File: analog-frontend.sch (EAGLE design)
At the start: 70 parts, among them IC1 TPS63031, IC2 ADG731, IC3 TM4C123G, IC4 INA332, IC5 NRF24L01SMD, IC6 OPA2320, Y1 CRYSTAL3X2, Y2 CRYSTAL3X2

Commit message: final files send for fab.
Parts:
- removed R16: (no value), FAB_Hello:RESISTOR0402
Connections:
- net AIN: now also IC3A.PB5; no longer IC5.PB5
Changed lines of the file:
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@@
 <part name="R3" library="rcl" deviceset="R-US_" device="R0402"/>
 <part name="SUPPLY25" library="supply2" deviceset="GND" device=""/>
-<part name="R16" library="FAB_Hello" deviceset="RESISTOR" device="0402"/>
 </parts>
 <sheets>
@@
 <instance part="R3" gate="G$1" x="149.86" y="68.58" rot="R90"/>
 <instance part="SUPPLY25" gate="GND" x="149.86" y="55.88"/>
-<instance part="R16" gate="G$1" x="116.84" y="149.86"/>
 </instances>
 <busses>
@@
 <wire x1="340.36" y1="233.68" x2="340.36" y2="226.06" width="0.1524" layer="91"/>
 <junction x="340.36" y="226.06"/>
+<label x="340.36" y="241.3" size="1.27" layer="95" rot="R90" xref="yes"/>
 <wire x1="340.36" y1="233.68" x2="340.36" y2="241.3" width="0.1524" layer="91"/>
 <junction x="340.36" y="233.68"/>
-<wire x1="340.36" y1="241.3" x2="342.9" y2="241.3" width="0.1524" layer="91"/>
-<label x="342.9" y="241.3" size="1.27" layer="95" xref="yes"/>
-</segment>
-<segment>
-<pinref part="IC5" gate="A" pin="PB5"/>
-<wire x1="213.36" y1="121.92" x2="220.98" y2="121.92" width="0.1524" layer="91"/>
-<label x="220.98" y="121.92" size="1.27" layer="95" xref="yes"/>
+</segment>
+<segment>
+<pinref part="IC3" gate="A" pin="PB5"/>
+<wire x1="213.36" y1="121.92" x2="223.52" y2="121.92" width="0.1524" layer="91"/>
+<wire x1="223.52" y1="121.92" x2="223.52" y2="134.62" width="0.1524" layer="91"/>
+<label x="223.52" y="134.62" size="1.27" layer="95" rot="R90" xref="yes"/>
 </segment>
 </net>
@@
 </segment>
 </net>
-<net name="N$57" class="0">
-<segment>
-<wire x1="228.6" y1="106.68" x2="228.6" y2="101.6" width="0.1524" layer="91"/>
-</segment>
-</net>

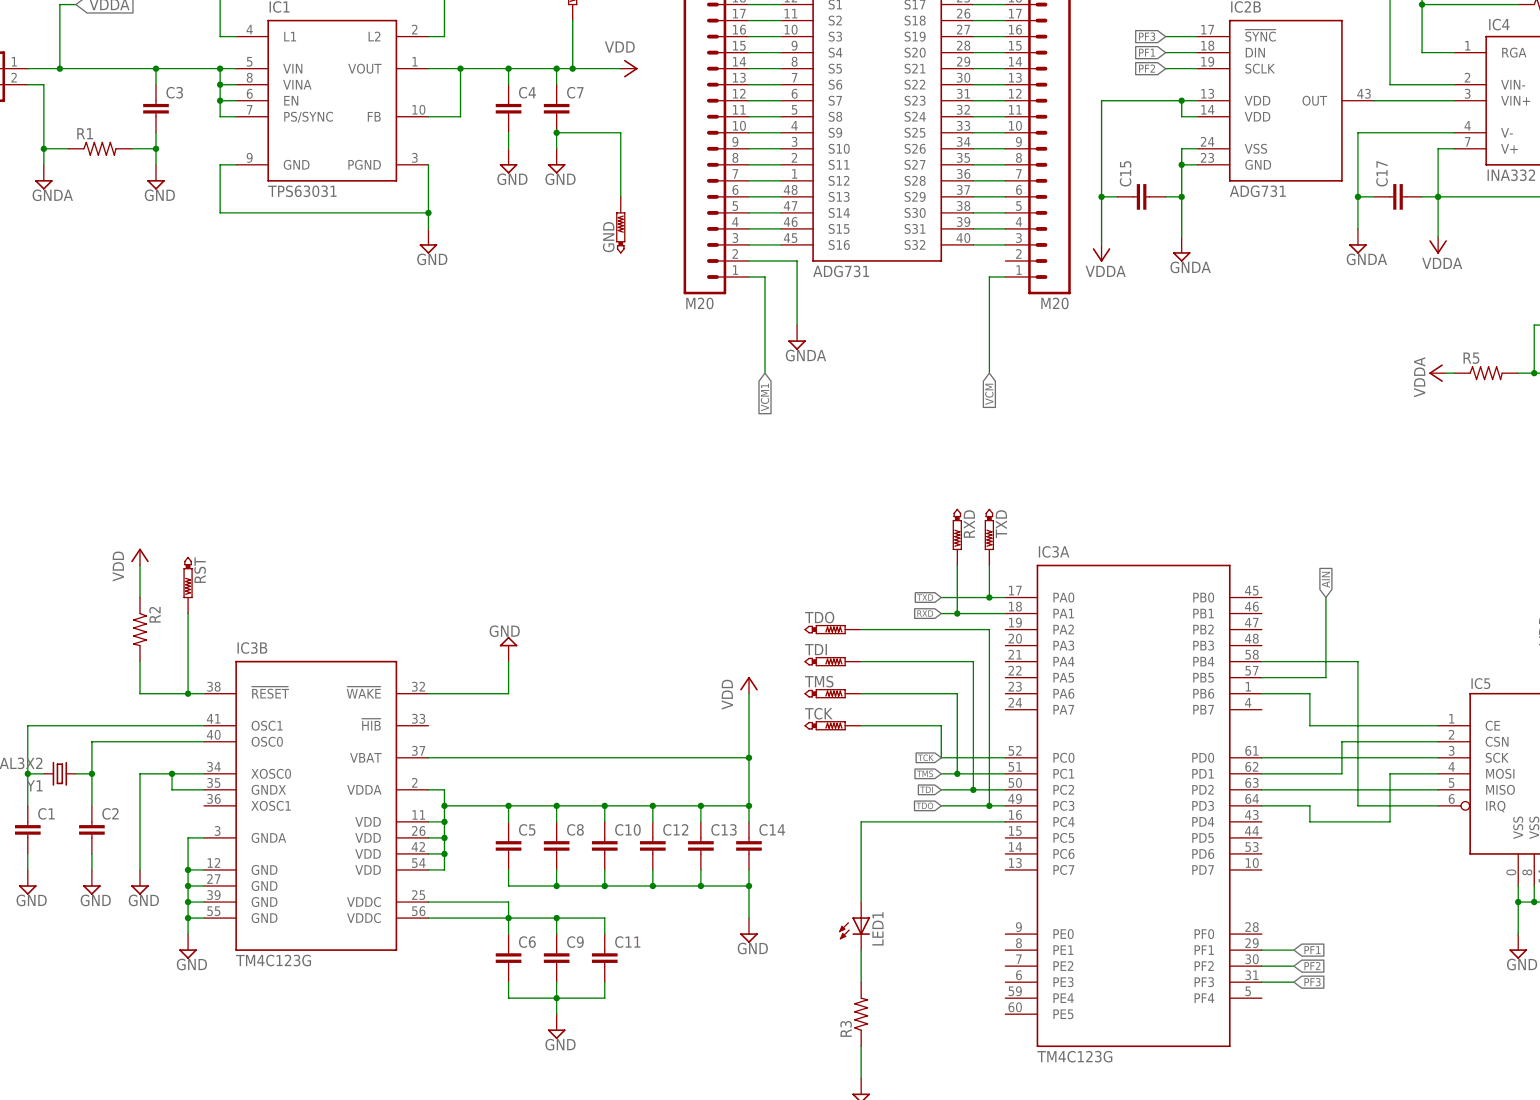
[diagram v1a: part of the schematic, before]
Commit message: added component values
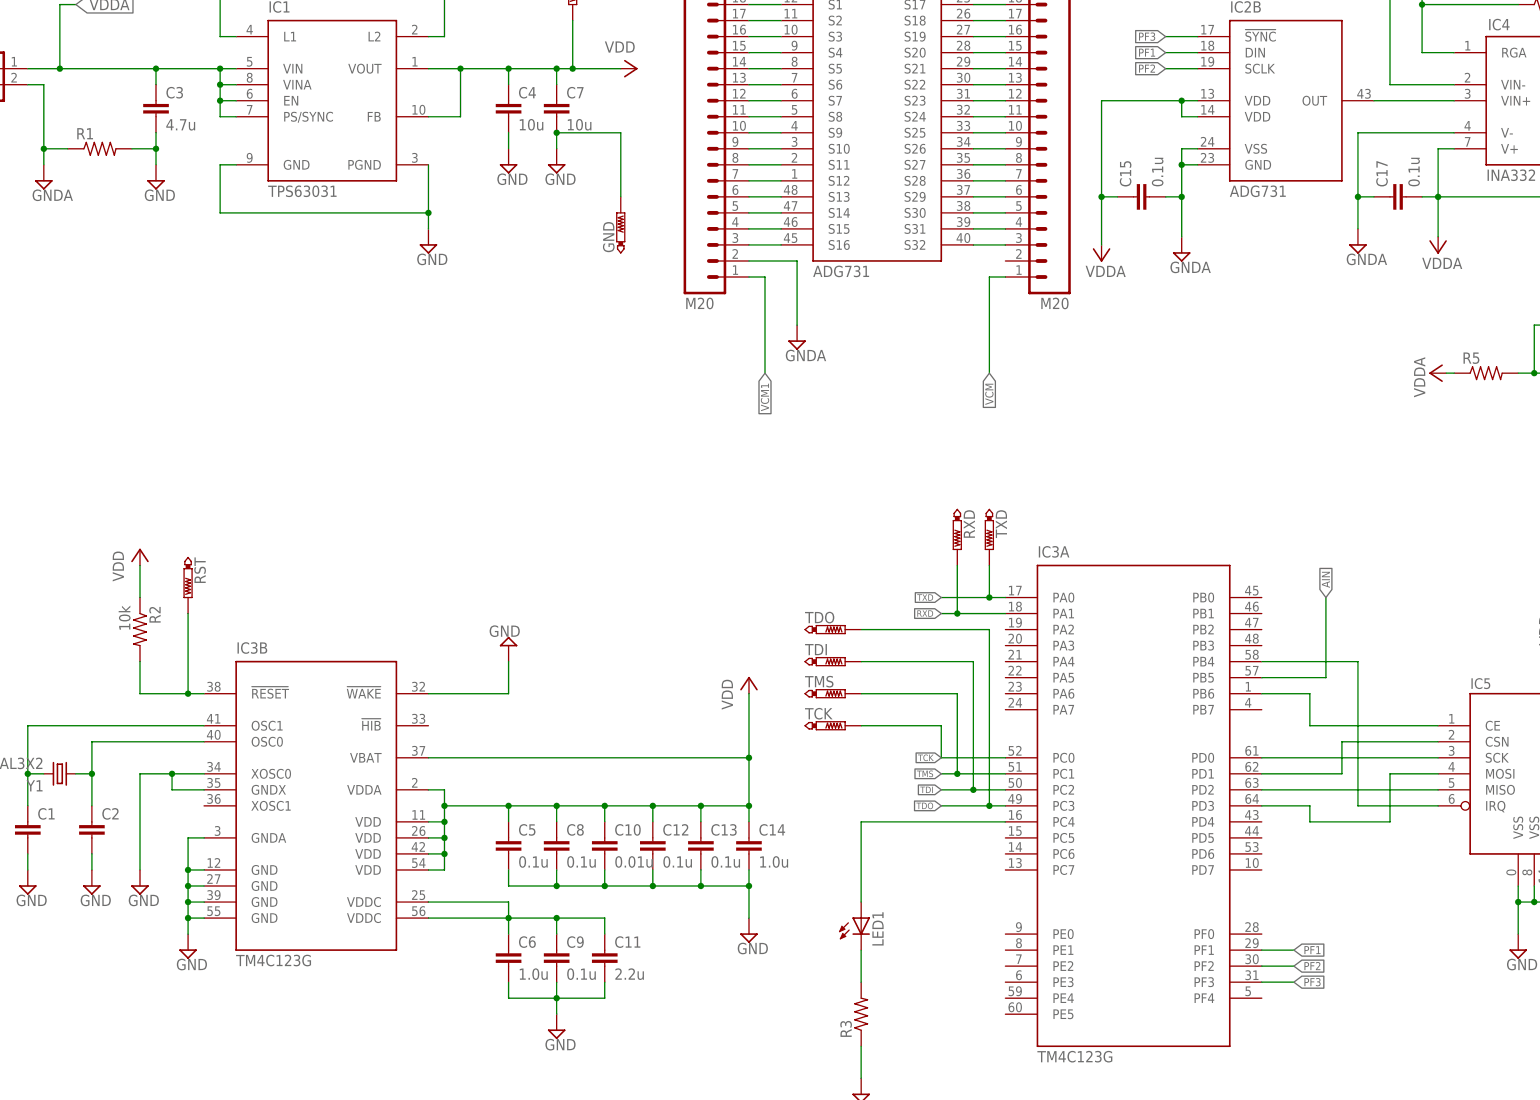
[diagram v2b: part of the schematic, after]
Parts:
- C10: value (none) -> 0.01u
- C11: value (none) -> 2.2u
- C12, C13, C15, C17, C5, C8, C9: value (none) -> 0.1u
- C14, C6: value (none) -> 1.0u
- C3: value (none) -> 4.7u
- C4, C7: value (none) -> 10u
- R2: value (none) -> 10k
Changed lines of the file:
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@@
 <?xml version="1.0" encoding="utf-8"?>
 <!DOCTYPE eagle SYSTEM "eagle.dtd">
-<eagle version="6.5.0">
+<eagle version="6.6.0">
 <drawing>
 <settings>
@@
 <part name="IC1" library="mor307" deviceset="TPS63031" device=""/>
 <part name="L1" library="mor307" deviceset="VLS25201" device=""/>
-<part name="C3" library="rcl" deviceset="C-EU" device="C0402"/>
-<part name="C4" library="rcl" deviceset="C-EU" device="C0402"/>
+<part name="C3" library="rcl" deviceset="C-EU" device="C0402" value="4.7u"/>
+<part name="C4" library="rcl" deviceset="C-EU" device="C0402" value="10u"/>
 <part name="SUPPLY1" library="supply2" deviceset="GND" device=""/>
 <part name="SUPPLY2" library="supply2" deviceset="GND" device=""/>
 <part name="SUPPLY3" library="supply2" deviceset="GND" device=""/>
-<part name="C7" library="rcl" deviceset="C-EU" device="C0402"/>
+<part name="C7" library="rcl" deviceset="C-EU" device="C0402" value="10u"/>
 <part name="SUPPLY4" library="supply2" deviceset="GND" device=""/>
 <part name="IC3" library="mor307" deviceset="TM4C123G" device=""/>
@@
 <part name="R11" library="rcl" deviceset="R-US_" device="R0402"/>
 <part name="C23" library="rcl" deviceset="C-EU" device="C0402"/>
-<part name="C17" library="rcl" deviceset="C-EU" device="C0402"/>
+<part name="C17" library="rcl" deviceset="C-EU" device="C0402" value="0.1u"/>
 <part name="SUPPLY5" library="supply2" deviceset="GND" device="" value="GNDA"/>
 <part name="C25" library="rcl" deviceset="C-EU" device="C0402"/>
@@
 <part name="+3V2" library="supply1" deviceset="+3V3" device="" value="VDDA"/>
 <part name="+3V3" library="supply1" deviceset="+3V3" device="" value="VDDA"/>
-<part name="C15" library="rcl" deviceset="C-EU" device="C0402"/>
+<part name="C15" library="rcl" deviceset="C-EU" device="C0402" value="0.1u"/>
 <part name="SUPPLY8" library="supply2" deviceset="GND" device="" value="GNDA"/>
 <part name="+3V4" library="supply1" deviceset="+3V3" device="" value="VDDA"/>
@@
 <part name="SUPPLY19" library="supply2" deviceset="GND" device=""/>
 <part name="SUPPLY20" library="supply2" deviceset="GND" device=""/>
-<part name="C6" library="rcl" deviceset="C-EU" device="C0402"/>
-<part name="C9" library="rcl" deviceset="C-EU" device="C0402"/>
-<part name="C11" library="rcl" deviceset="C-EU" device="C0402"/>
+<part name="C6" library="rcl" deviceset="C-EU" device="C0402" value="1.0u"/>
+<part name="C9" library="rcl" deviceset="C-EU" device="C0402" value="0.1u"/>
+<part name="C11" library="rcl" deviceset="C-EU" device="C0402" value="2.2u"/>
 <part name="SUPPLY21" library="supply2" deviceset="GND" device=""/>
-<part name="C5" library="rcl" deviceset="C-EU" device="C0402"/>
-<part name="C8" library="rcl" deviceset="C-EU" device="C0402"/>
-<part name="C10" library="rcl" deviceset="C-EU" device="C0402"/>
-<part name="C12" library="rcl" deviceset="C-EU" device="C0402"/>
-<part name="C13" library="rcl" deviceset="C-EU" device="C0402"/>
-<part name="C14" library="rcl" deviceset="C-EU" device="C0402"/>
+<part name="C5" library="rcl" deviceset="C-EU" device="C0402" value="0.1u"/>
+<part name="C8" library="rcl" deviceset="C-EU" device="C0402" value="0.1u"/>
+<part name="C10" library="rcl" deviceset="C-EU" device="C0402" value="0.01u"/>
+<part name="C12" library="rcl" deviceset="C-EU" device="C0402" value="0.1u"/>
+<part name="C13" library="rcl" deviceset="C-EU" device="C0402" value="0.1u"/>
+<part name="C14" library="rcl" deviceset="C-EU" device="C0402" value="1.0u"/>
 <part name="+3V7" library="supply1" deviceset="+3V3" device="" value="VDD"/>
 <part name="SUPPLY22" library="supply2" deviceset="GND" device=""/>
-<part name="R2" library="rcl" deviceset="R-US_" device="R0402"/>
+<part name="R2" library="rcl" deviceset="R-US_" device="R0402" value="10k"/>
 <part name="+3V8" library="supply1" deviceset="+3V3" device="" value="VDD"/>
 <part name="SUPPLY23" library="supply2" deviceset="GND" device=""/>
